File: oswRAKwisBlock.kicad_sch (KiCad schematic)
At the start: 38 parts, among them J1 WisBlock, J2 0524352471, J4 10114830-10102LF, J5 USB micro, Q1 SI1308EDL-T1-GE3, U1 MCP73811T-420I/OT, U5 MIC5365-3.0YC5-TR

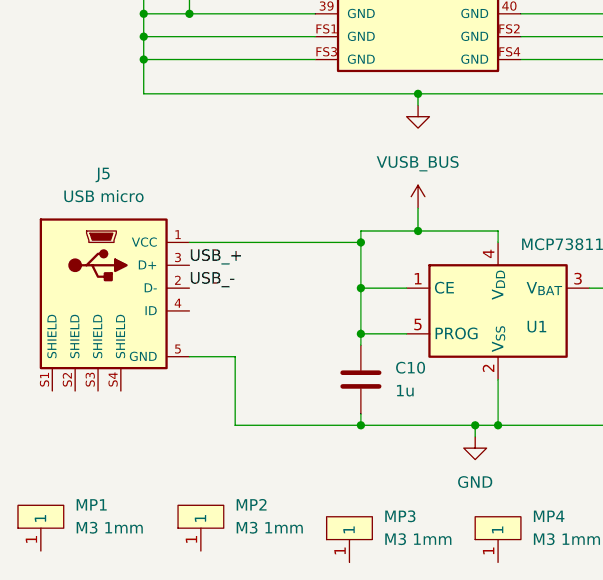
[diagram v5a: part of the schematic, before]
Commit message: Mirroring layout to match watchy layout better.
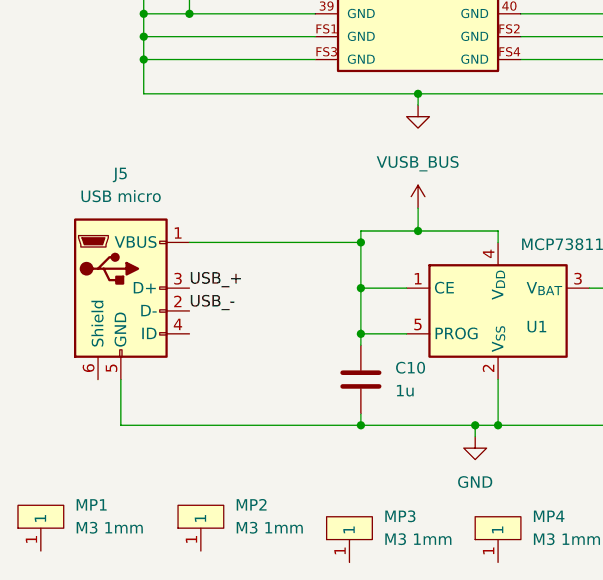
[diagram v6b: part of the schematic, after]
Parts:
- J5: footprint AllardConnFootPrints:GCT_USB3190-GF-C -> AllardFootPrints:GCT_USB3075-30-A; symbol AllardConn:J10033 -> AllardConn:J10001; AI_PN (none) -> ${SYMBOL_NAME}; MPN USB3190-GF-C -> USB3075-30-A; SUP1 DigiKey -> Digi-Key; SUP1_PN 2073-USB3190-GF-CCT-ND -> 2073-USB3075-30-ACT-ND; SUP2_PN 640-USB3190-GF-C -> 640-USB3075-30-A; manf# USB3190-GF-C -> USB3075-30-A
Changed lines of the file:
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@@
 	(wire
 		(pts
-			(xy 111.76 60.96) (xy 114.3 60.96)
+			(xy 35.56 163.83) (xy 35.56 168.91)
 		)
 		(stroke
@@
 	(wire
 		(pts
-			(xy 62.23 168.91) (xy 48.26 168.91)
+			(xy 111.76 60.96) (xy 114.3 60.96)
 		)
 		(stroke
@@
 	(wire
 		(pts
-			(xy 48.26 161.29) (xy 43.18 161.29)
+			(xy 35.56 168.91) (xy 62.23 168.91)
 		)
 		(stroke
@@
 	(wire
 		(pts
-			(xy 48.26 168.91) (xy 48.26 161.29)
-		)
-		(stroke
-			(width 0)
-			(type default)
-		)
-	)
-	(wire
-		(pts
 			(xy 80.01 80.01) (xy 96.52 80.01)
 		)
@@
 	)
 	(label "USB_-"
-		(at 43.18 153.67 0)
+		(at 43.18 156.21 0)
 		(fields_autoplaced yes)
 		(effects
@@
 	)
 	(label "USB_+"
-		(at 43.18 151.13 0)
+		(at 43.18 153.67 0)
 		(fields_autoplaced yes)
 		(effects
@@
 	)
 	(symbol
-		(lib_id "AllardConn:J10033")
-		(at 30.48 157.48 0)
+		(lib_id "AllardConn:J10001")
+		(at 35.56 153.67 0)
 		(unit 1)
 		(exclude_from_sim no)
@@
 		(fields_autoplaced yes)
 		(property "Reference" "J5"
-			(at 33.655 140.97 0)
+			(at 35.56 140.97 0)
 			(effects
 				(font
@@
 		)
 		(property "Value" "USB micro"
-			(at 33.655 143.51 0)
+			(at 35.56 143.51 0)
 			(effects
 				(font
@@
 			)
 		)
-		(property "Footprint" "AllardConnFootPrints:GCT_USB3190-GF-C"
-			(at 33.02 178.816 0)
+		(property "Footprint" "AllardFootPrints:GCT_USB3075-30-A"
+			(at 39.37 154.94 0)
 			(effects
 				(font
 					(size 1.27 1.27)
 				)
-				(justify bottom)
 				(hide yes)
 			)
 		)
-		(property "Datasheet" "https://gct.co/files/specs/usb3190-spec.pdf"
-			(at 32.766 188.468 0)
+		(property "Datasheet" "http://www.farnell.com/datasheets/2342961.pdf"
+			(at 39.37 154.94 0)
 			(effects
 				(font
@@
 			)
 		)
-		(property "Description" "MICRO B SKT VERT MID MOUNT H=3.9"
-			(at 32.766 188.468 0)
+		(property "Description" "USB Micro Type B connector"
+			(at 35.56 153.67 0)
 			(effects
 				(font
@@
 			)
 		)
-		(property "MPN" "USB3190-GF-C"
-			(at 32.766 188.468 0)
+		(property "MPN" "USB3075-30-A"
+			(at 35.56 153.67 0)
 			(effects
 				(font
-					(size 1.27 1.27)
+					(size 1.2446 1.2446)
 				)
-				(justify bottom)
 				(hide yes)
 			)
 		)
-		(property "manf#" "USB3190-GF-C"
-			(at 22.352 181.102 0)
+		(property "manf#" "USB3075-30-A"
+			(at 36.83 143.51 0)
 			(effects
 				(font
 					(size 1.27 1.27)
 				)
-				(justify bottom)
 				(hide yes)
 			)
 		)
-		(property "SUP1" "DigiKey"
-			(at 37.084 180.594 0)
+		(property "SUP1" "Digi-Key"
+			(at 35.56 153.67 0)
 			(effects
 				(font
-					(size 1.27 1.27)
+					(size 1.2446 1.2446)
 				)
-				(justify bottom)
 				(hide yes)
 			)
 		)
-		(property "SUP1_PN" "2073-USB3190-GF-CCT-ND"
-			(at 30.734 179.832 0)
+		(property "SUP1_PN" "2073-USB3075-30-ACT-ND"
+			(at 35.56 153.67 0)
 			(effects
 				(font
-					(size 1.27 1.27)
+					(size 1.2446 1.2446)
 				)
-				(justify bottom)
 				(hide yes)
 			)
 		)
 		(property "SUP2" "Mouser"
-			(at 33.02 178.816 0)
+			(at 35.56 153.67 0)
 			(effects
 				(font
-					(size 1.27 1.27)
+					(size 1.2446 1.2446)
 				)
-				(justify bottom)
 				(hide yes)
 			)
 		)
-		(property "SUP2_PN" "640-USB3190-GF-C"
-			(at 33.02 178.816 0)
+		(property "SUP2_PN" "640-USB3075-30-A"
+			(at 35.56 153.67 0)
 			(effects
 				(font
-					(size 1.27 1.27)
+					(size 1.2446 1.2446)
 				)
-				(justify bottom)
 				(hide yes)
 			)
 		)
 		(property "SUP3" "LCSC"
-			(at 32.766 188.468 0)
+			(at 37.846 184.658 0)
 			(effects
 				(font
@@
 		)
 		(property "SUP3_PN" "C7407277"
-			(at 33.02 178.816 0)
+			(at 38.1 175.006 0)
 			(effects
 				(font
@@
 		)
 		(property "Temperature" "-30°C ~ 85°C"
-			(at 33.02 178.816 0)
+			(at 38.1 175.006 0)
 			(effects
 				(font
@@
 		)
 		(property "variant" "default"
-			(at 33.02 178.816 0)
+			(at 35.56 153.67 0)
 			(effects
 				(font
 					(size 1.27 1.27)
 				)
-				(justify bottom)
 				(hide yes)
 			)
 		)
 		(property "Manufacturer" "GCT"
-			(at 32.766 188.468 0)
+			(at 35.56 153.67 0)
 			(effects
 				(font
-					(size 1.27 1.27)
+					(size 1.2446 1.2446)
+				)
+				(hide yes)
+			)
+		)
+		(property "AI_PN" "${SYMBOL_NAME}"
+			(at 35.56 153.67 0)
+			(effects
+				(font
+					(size 1.2446 1.2446)
 				)
-				(justify bottom)
 				(hide yes)
 			)
@@
 		(pin "4"
 		)
-		(pin "S1"
-		)
-		(pin "S4"
+		(pin "6"
 		)
 		(pin "3"
 		)
-		(pin "S2"
-		)
-		(pin "S3"
-		)
 		(pin "2"

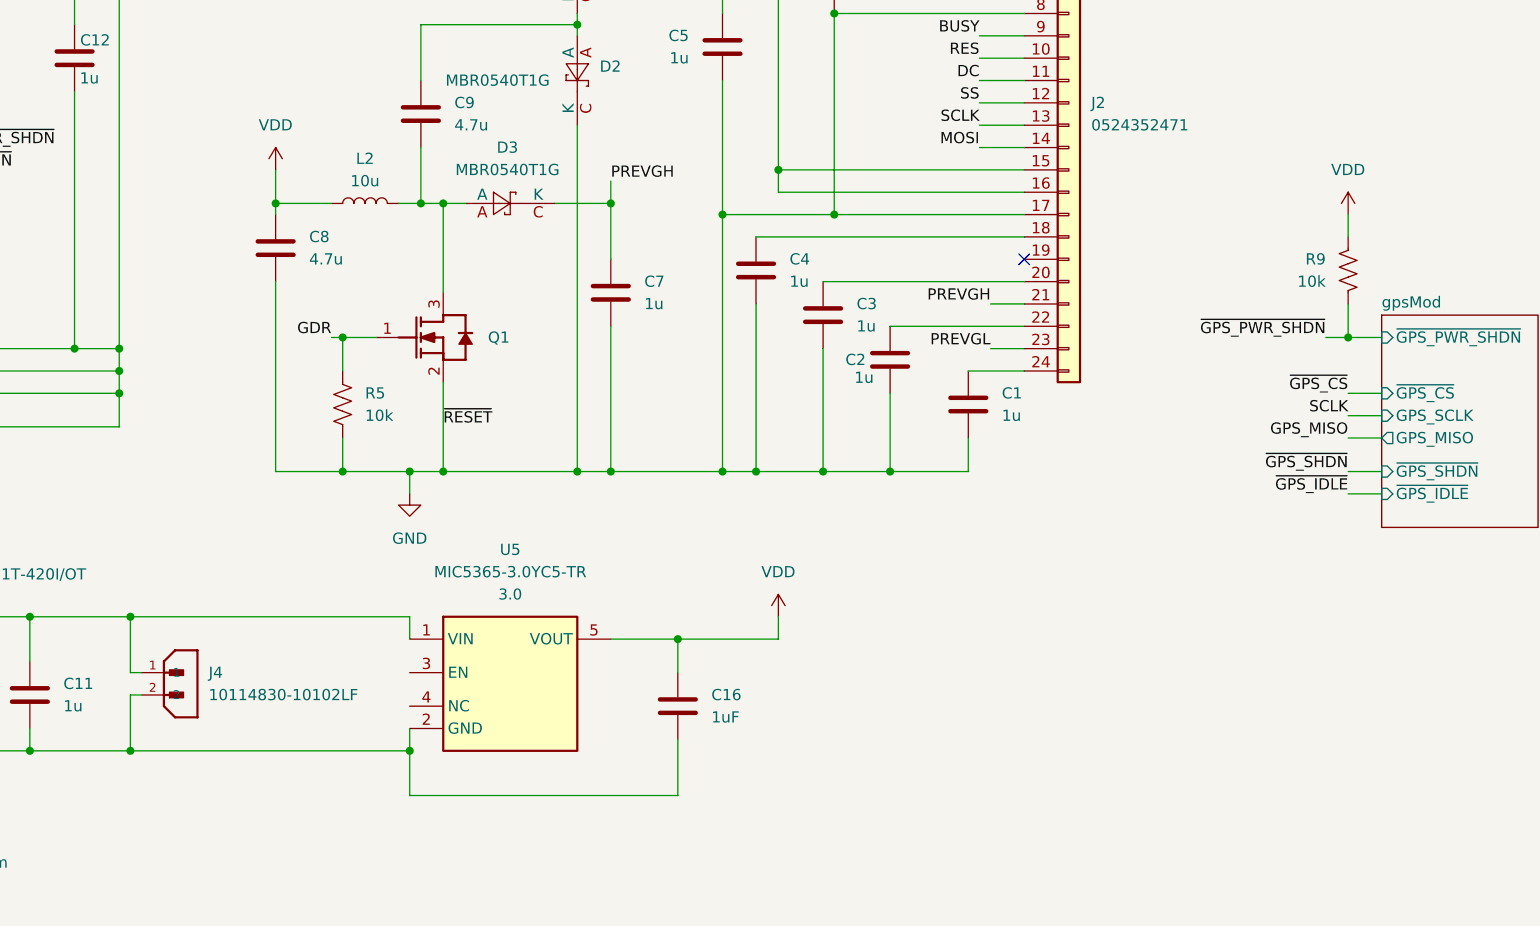
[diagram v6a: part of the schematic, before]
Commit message: Adding mounting holes.
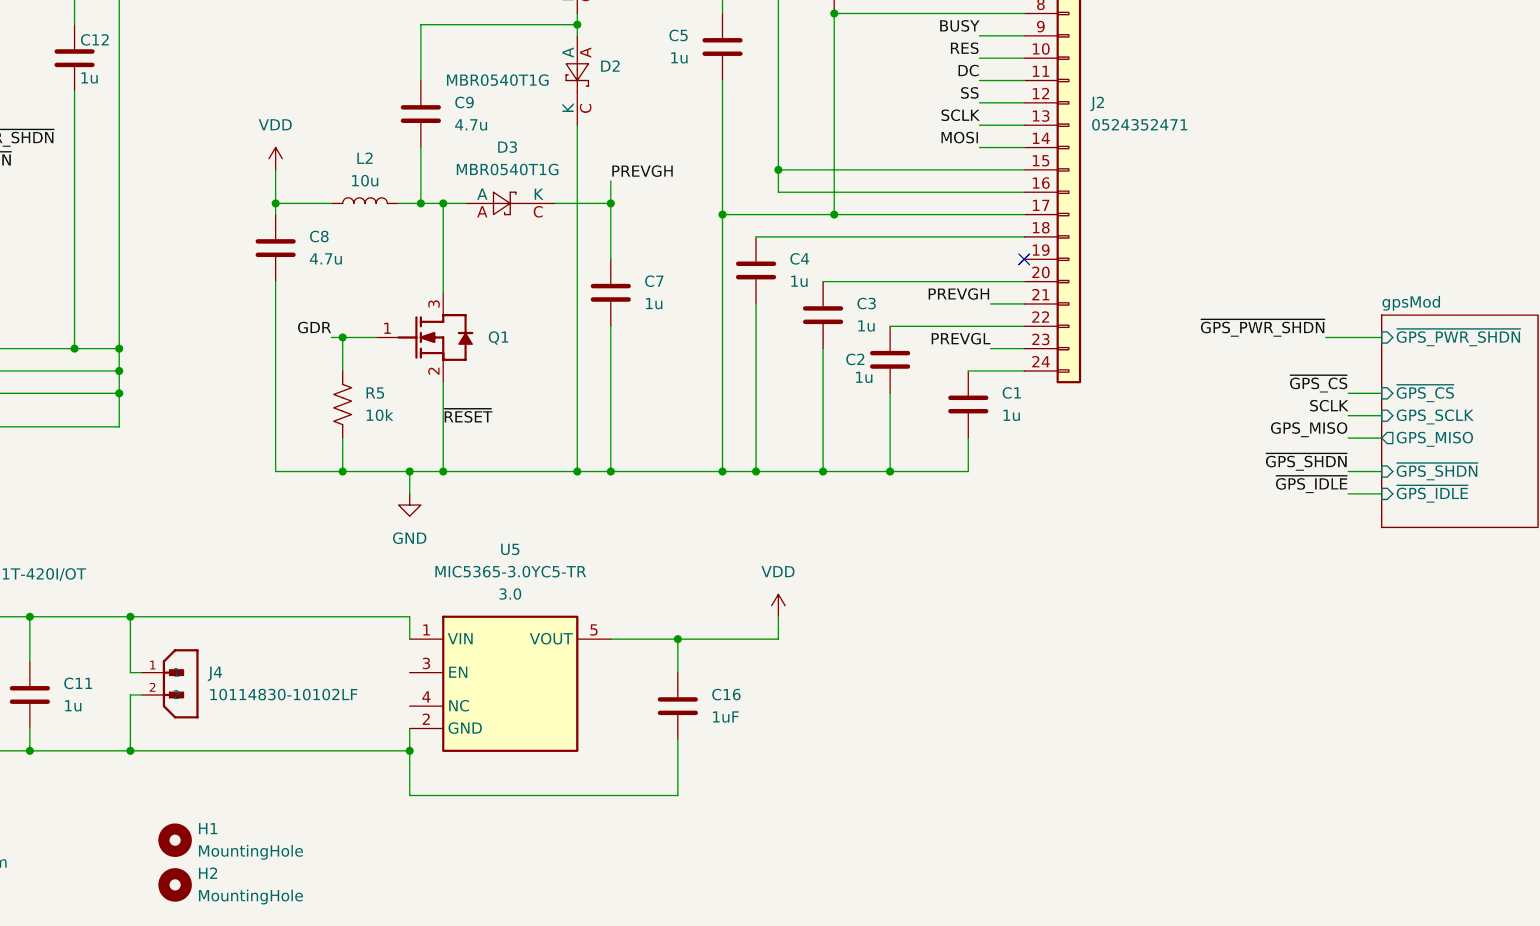
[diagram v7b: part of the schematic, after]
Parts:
- removed R9: 10k, AllardChip:RESC40X20X15L10L, symbol AllardPassive:R10020-10000
- added H1, H2: MountingHole, MountingHole:MountingHole_2.2mm_M2, symbol Mechanical:MountingHole
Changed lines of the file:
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@@
 	)
 	(junction
-		(at 241.3 121.92)
-		(diameter 0)
-		(color 0 0 0 0)
-	)
-	(junction
 		(at 111.76 44.45)
 		(diameter 0)
@@
 	(wire
 		(pts
-			(xy 241.3 107.95) (xy 241.3 110.49)
-		)
-		(stroke
-			(width 0)
-			(type default)
-		)
-	)
-	(wire
-		(pts
 			(xy 57.15 102.87) (xy 45.72 102.87)
 		)
@@
 	(wire
 		(pts
-			(xy 238.76 121.92) (xy 241.3 121.92)
+			(xy 238.76 121.92) (xy 245.11 121.92)
 		)
 		(stroke
@@
 	(wire
 		(pts
-			(xy 241.3 121.92) (xy 245.11 121.92)
-		)
-		(stroke
-			(width 0)
-			(type default)
-		)
-	)
-	(wire
-		(pts
 			(xy 38.1 125.73) (xy 57.15 125.73)
 		)
@@
 	(wire
 		(pts
-			(xy 241.3 118.11) (xy 241.3 121.92)
-		)
-		(stroke
-			(width 0)
-			(type default)
-		)
-	)
-	(wire
-		(pts
 			(xy 119.38 115.57) (xy 119.38 137.16)
 		)
@@
 	)
 	(symbol
-		(lib_id "power:VDD")
-		(at 241.3 107.95 0)
+		(lib_id "Mechanical:MountingHole")
+		(at 107.95 179.07 0)
 		(unit 1)
-		(exclude_from_sim no)
-		(in_bom yes)
+		(exclude_from_sim yes)
+		(in_bom no)
 		(on_board yes)
 		(dnp no)
 		(fields_autoplaced yes)
-		(property "Reference" "#PWR019"
-			(at 241.3 111.76 0)
+		(property "Reference" "H1"
+			(at 110.49 177.7999 0)
 			(effects
 				(font
 					(size 1.27 1.27)
 				)
-				(hide yes)
+				(justify left)
 			)
 		)
-		(property "Value" "VDD"
-			(at 241.3 102.87 0)
+		(property "Value" "MountingHole"
+			(at 110.49 180.3399 0)
 			(effects
 				(font
 					(size 1.27 1.27)
 				)
+				(justify left)
 			)
 		)
-		(property "Footprint" ""
-			(at 241.3 107.95 0)
+		(property "Footprint" "MountingHole:MountingHole_2.2mm_M2"
+			(at 107.95 179.07 0)
 			(effects
 				(font
@@
 			)
 		)
-		(property "Datasheet" ""
-			(at 241.3 107.95 0)
+		(property "Datasheet" "~"
+			(at 107.95 179.07 0)
 			(effects
 				(font
@@
 			)
 		)
-		(property "Description" "Power symbol creates a global label with name \"VDD\""
-			(at 241.3 107.95 0)
+		(property "Description" "Mounting Hole without connection"
+			(at 107.95 179.07 0)
 			(effects
 				(font
@@
 			)
 		)
-		(pin "1"
-		)
 		(instances
 			(project "oswRAKwisBlock"
 				(path "/2fe076e6-bb0e-436f-836d-ec5f0ee79cef"
-					(reference "#PWR019")
+					(reference "H1")
 					(unit 1)
 				)
@@
 	)
 	(symbol
-		(lib_id "AllardPassive:R10020-10000")
-		(at 241.3 114.3 0)
-		(mirror y)
-		(unit 1)
-		(exclude_from_sim no)
-		(in_bom yes)
-		(on_board yes)
-		(dnp no)
-		(property "Reference" "R9"
-			(at 238.76 113.0299 0)
-			(effects
-				(font
-					(size 1.27 1.27)
-				)
-				(justify left)
-			)
-		)
-		(property "Value" "10k"
-			(at 238.76 115.5699 0)
-			(effects
-				(font
-					(size 1.27 1.27)
-				)
-				(justify left)
-			)
-		)
-		(property "Footprint" "AllardChip:RESC40X20X15L10L"
-			(at 240.284 114.554 90)
-			(effects
-				(font
-					(size 1.27 1.27)
-				)
-				(hide yes)
-			)
-		)
-		(property "Datasheet" "https://industrial.panasonic.com/cdbs/www-data/pdf/RDA0000/AOA0000C304.pdf"
-			(at 241.3 114.3 0)
-			(effects
-				(font
-					(size 1.27 1.27)
-				)
-				(hide yes)
-			)
-		)
-		(property "Description" "10k 01005 0.03W 1% Res"
-			(at 241.3 114.3 0)
-			(effects
-				(font
-					(size 1.27 1.27)
-				)
-				(hide yes)
-			)
-		)
-		(property "AI_PN" "${SYMBOL_NAME}"
-			(at 241.3 114.3 0)
-			(effects
-				(font
-					(size 1.2446 1.2446)
-				)
-				(hide yes)
-			)
-		)
-		(property "MPN" "ERJ-XGNF1002Y"
-			(at 241.3 114.3 0)
-			(effects
-				(font
-					(size 1.2446 1.2446)
-				)
-				(hide yes)
-			)
-		)
-		(property "Manufacturer" "Panasonic Electronics Components"
-			(at 241.3 114.3 0)
-			(effects
-				(font
-					(size 1.2446 1.2446)
-				)
-				(hide yes)
-			)
-		)
-		(property "manf#" "ERJ-XGNF1002Y"
-			(at 241.3 114.3 0)
-			(effects
-				(font
-					(size 1.2446 1.2446)
-				)
-				(hide yes)
-			)
-		)
-		(property "SUP1" "Digi-Key"
-			(at 241.3 114.3 0)
-			(effects
-				(font
-					(size 1.2446 1.2446)
-				)
-				(hide yes)
-			)
-		)
-		(property "SUP1_PN" "10-ERJ-XGNF1002YCT-ND"
-			(at 241.3 114.3 0)
-			(effects
-				(font
-					(size 1.2446 1.2446)
-				)
-				(hide yes)
-			)
-		)
-		(property "SUP2" "Mouser"
-			(at 241.3 114.3 0)
-			(effects
-				(font
-					(size 1.2446 1.2446)
-				)
-				(hide yes)
-			)
-		)
-		(property "SUP2_PN" "667-ERJ-XGNF1002Y"
-			(at 241.3 114.3 0)
-			(effects
-				(font
-					(size 1.2446 1.2446)
-				)
-				(hide yes)
-			)
-		)
-		(property "Tolerance" "1%"
-			(at 241.3 114.3 0)
-			(effects
-				(font
-					(size 1.2446 1.2446)
-				)
-				(hide yes)
-			)
-		)
-		(property "Power" "0.03W"
-			(at 241.3 114.3 0)
-			(effects
-				(font
-					(size 1.2446 1.2446)
-				)
-				(hide yes)
-			)
-		)
-		(property "Temperature" "-55-125"
-			(at 241.3 114.3 0)
-			(effects
-				(font
-					(size 1.2446 1.2446)
-				)
-				(hide yes)
-			)
-		)
-		(property "variant" "default"
-			(at 241.3 114.3 0)
-			(effects
-				(font
-					(size 1.27 1.27)
-				)
-				(hide yes)
-			)
-		)
-		(property "TempCoef" "±200ppm/°C"
-			(at 241.3 114.3 0)
-			(effects
-				(font
-					(size 1.27 1.27)
-				)
-				(hide yes)
-			)
-		)
-		(pin "1"
-		)
-		(pin "2"
-		)
-		(instances
-			(project "oswRAKwisBlock"
-				(path "/2fe076e6-bb0e-436f-836d-ec5f0ee79cef"
-					(reference "R9")
-					(unit 1)
-				)
-			)
-		)
-	)
-	(symbol
 		(lib_id "power:GND")
 		(at 74.93 170.18 0)
@@
 					(unit 1)
 				)
+			)
+		)
+	)
+	(symbol
+		(lib_id "Mechanical:MountingHole")
+		(at 107.95 184.15 0)
+		(unit 1)
+		(exclude_from_sim yes)
+		(in_bom no)
+		(on_board yes)
+		(dnp no)
+		(fields_autoplaced yes)
+		(property "Reference" "H2"
+			(at 110.49 182.8799 0)
+			(effects
+				(font
+					(size 1.27 1.27)
+				)
+				(justify left)
+			)
+		)
+		(property "Value" "MountingHole"
+			(at 110.49 185.4199 0)
+			(effects
+				(font
+					(size 1.27 1.27)
+				)
+				(justify left)
+			)
+		)
+		(property "Footprint" "MountingHole:MountingHole_2.2mm_M2"
+			(at 107.95 184.15 0)
+			(effects
+				(font
+					(size 1.27 1.27)
+				)
+				(hide yes)
+			)
+		)
+		(property "Datasheet" "~"
+			(at 107.95 184.15 0)
+			(effects
+				(font
+					(size 1.27 1.27)
+				)
+				(hide yes)
+			)
+		)
+		(property "Description" "Mounting Hole without connection"
+			(at 107.95 184.15 0)
+			(effects
+				(font
+					(size 1.27 1.27)
+				)
+				(hide yes)
+			)
+		)
+		(instances
+			(project "oswRAKwisBlock"
+				(path "/2fe076e6-bb0e-436f-836d-ec5f0ee79cef"
+					(reference "H2")
+					(unit 1)
+				)

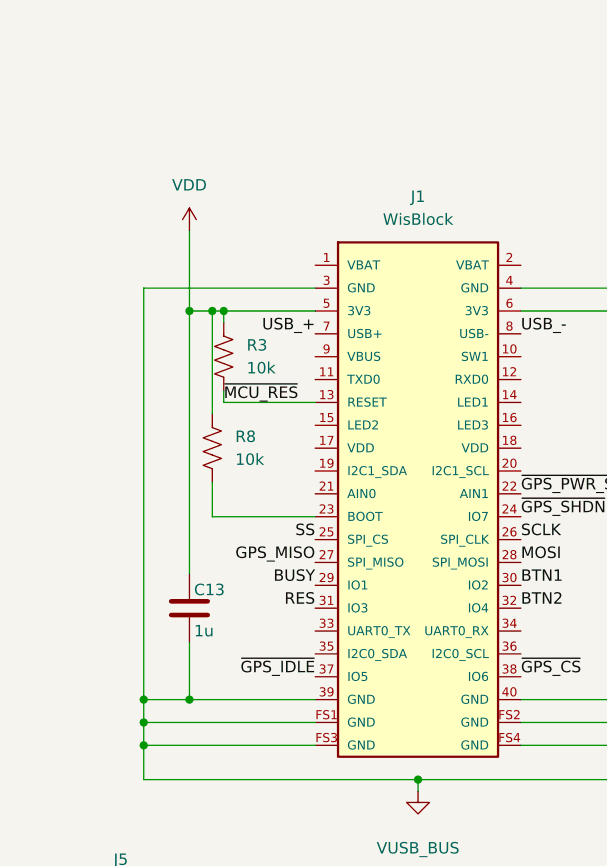
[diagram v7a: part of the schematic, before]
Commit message: Forgot to put the VBUS connection to the RAK mod.  Done now.
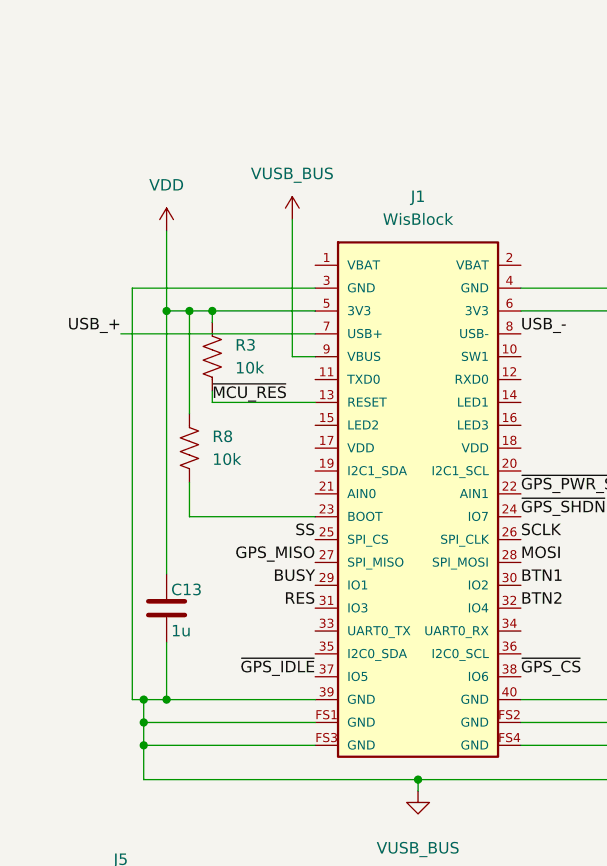
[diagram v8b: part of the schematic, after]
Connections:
- net VUSB_BUS: now also J1.9 (VBUS)
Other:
- moved on the sheet: C13, R3, R8
